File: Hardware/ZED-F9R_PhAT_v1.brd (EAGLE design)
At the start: 65 x 57.3 mm, 122 parts, among them J1 U.FL, J5 QWIIC_RIGHT_ANGLE, J6 RASPBERRYPI-40-PIN-GPIO_SMD_S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, U1 U-BLOX_ZED_F9R, U2 DUAL-OPTO_HCPL-073LSOIC-8, U3 UHS_INVERTER_SCHMITT_TRIGGER_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, U4 UHS_INVERTER_SCHMITT_TRIGGER_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

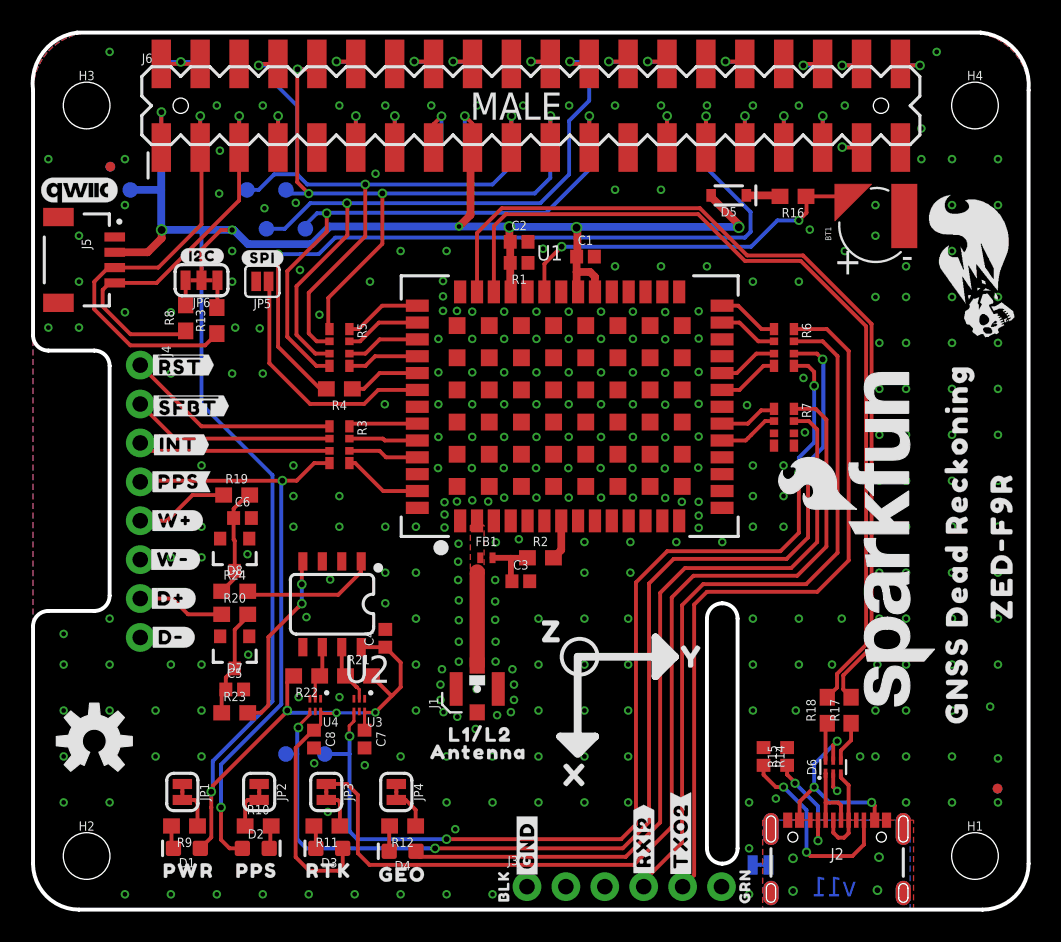
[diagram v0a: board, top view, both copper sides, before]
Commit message: Updates F9R module, Fixes various trace overlaps and acid traps
* Updates resistor values on LEDs
* Adds more capacitance to power lines
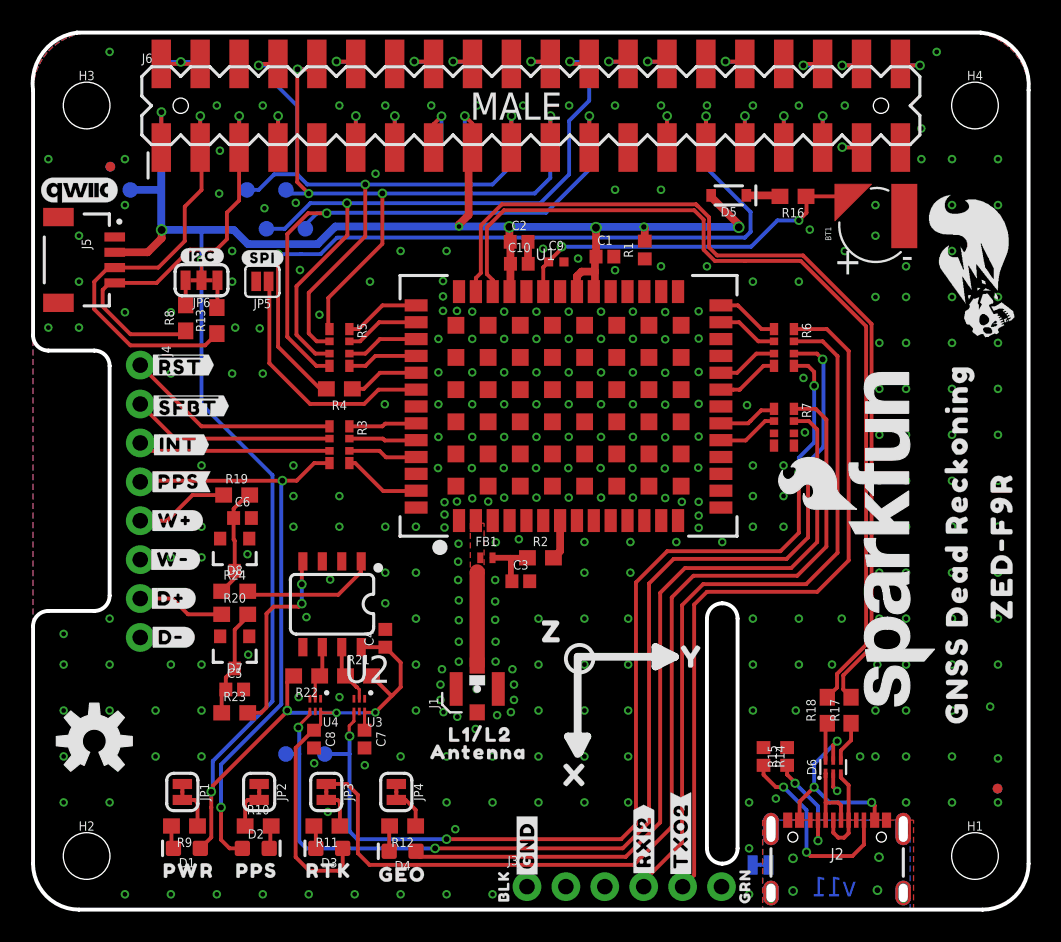
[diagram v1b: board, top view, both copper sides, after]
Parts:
- added C10: 1.0uF, SparkFun-Capacitors:0402
- added C9: 2.2uF, SparkFun-Capacitors:0402-TIGHT
- J2: device SparkFun-Connectors:USB-C-16P -> SparkFun-Connectors:USB-C-16P-2LAYER-PADS
- R10, R11, R12: value 4.7k -> 2.2k
- U1: value U-BLOX_ZED_F9R -> U-BLOX_ZED-F9R
- moved R1 8.25 mm to (39.9, 43.1), turned to 90 degrees
- moved C1 1.27 mm to (37.3, 42.6)
- moved U1 0.08 mm to (34.9, 33.0)
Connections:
- net 3.3V: now also C10.1
- net GND: now also C10.2, C9.2
- net SHIELD: no longer J2.SHLD5, J2.SHLD6, J2.SHLD7, J2.SHLD8
- net V_BATT: now also C9.1
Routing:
- net 3.3V: track 170.2 -> 167.4 mm, vias 12 -> 13
- net DMINUS: track 57.2 -> 59.1 mm
- net DPLUS: track 58.8 -> 60.3 mm
- net GND: track 1.23 -> 2.69 mm, vias 311 -> 312
- net QWIIC_SCL: track 26.4 -> 27.4 mm
- net DIR_IN: track 11.9 -> 12.9 mm
- net SCL/CLK: track 38.5 -> 39.2 mm
